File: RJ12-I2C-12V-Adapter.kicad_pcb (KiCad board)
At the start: 2 copper layers, 25.4 x 45.7 mm, 8 parts, among them J1 6P6C, J10 I²C, J11 Relais-Power, J2 6P6C

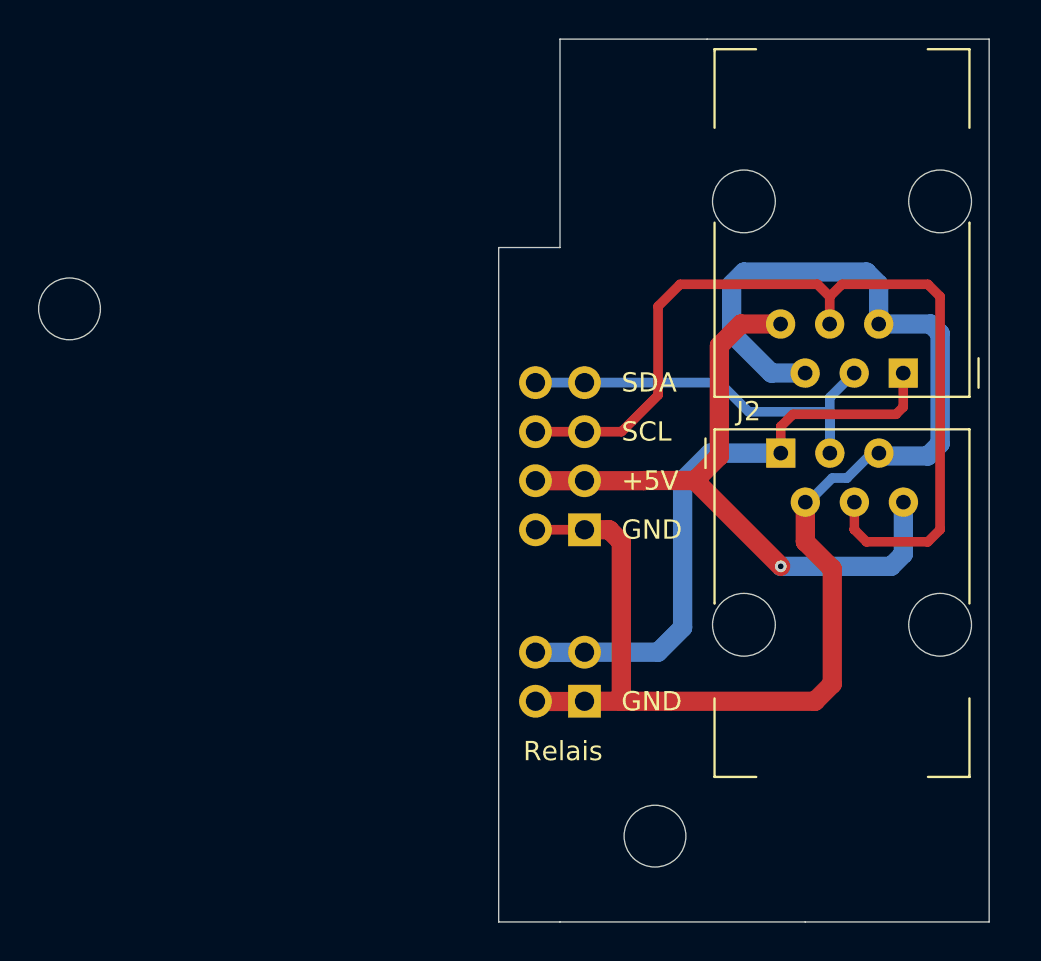
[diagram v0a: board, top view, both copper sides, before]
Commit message: Extra Anschlüsse für 12V/GND, RJ12 ganz an den Rand geschoben
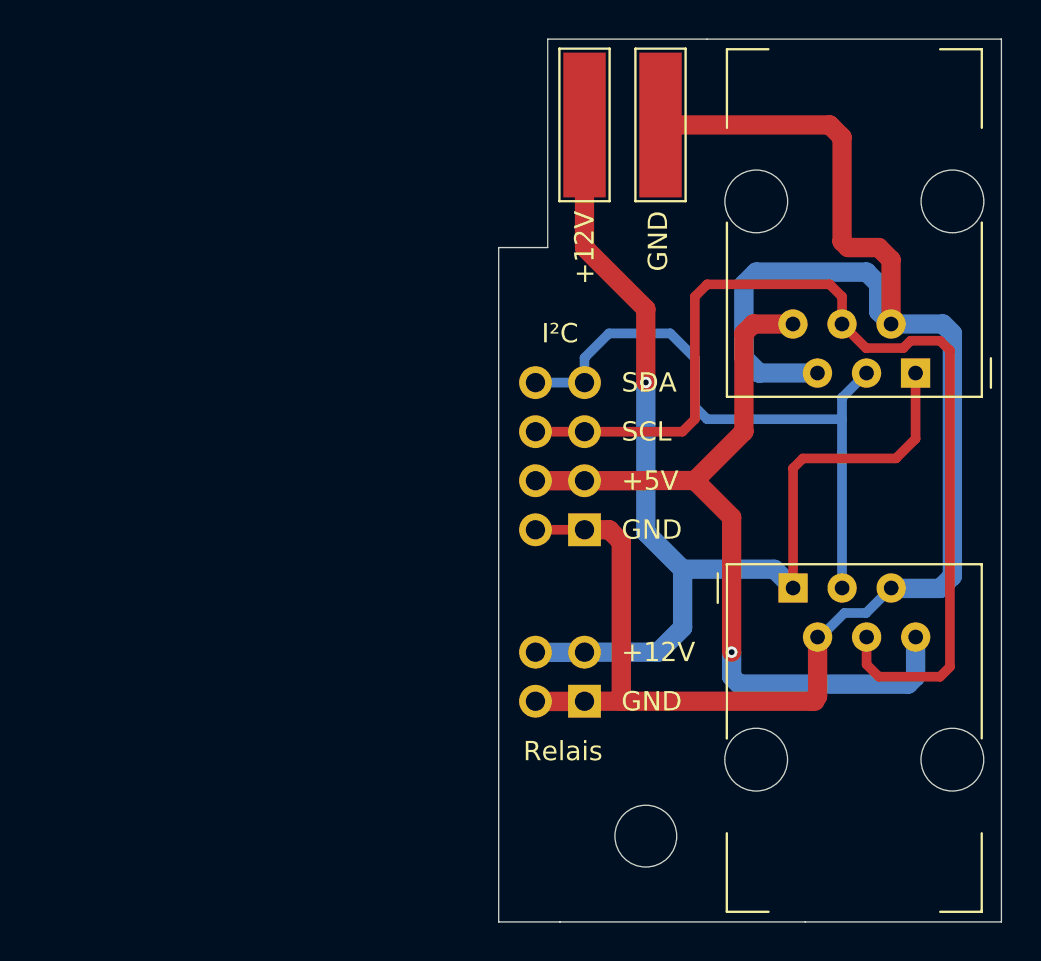
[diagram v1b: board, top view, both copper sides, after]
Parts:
- removed H1: MountingHole, MountingHole:MountingHole_3.2mm_M3
- added J12: +12V, Wago:Pad_7.5x2.2mm, F.Cu at (96.5, 71.8)
- added J13: GND, Wago:Pad_7.5x2.2mm, F.Cu at (100.5, 71.8)
- moved Tx1 21.1 mm to (81.3, 95.2)
- moved J2 7.01 mm to (107.3, 95.7)
- moved Tx2 3.67 mm to (106.7, 116.8)
- moved J1 0.64 mm to (113.7, 84.6)
- moved H2 0.48 mm to (99.7, 108.6)
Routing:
- net +12V: track 31.3 -> 59.0 mm, vias 0 -> 1
- net GND: track 73.4 -> 94.1 mm
- net /SDA: track 22.7 -> 32.7 mm
- net +5V: track 35.0 -> 42.4 mm
- net /SCL: track 47.5 -> 53.5 mm
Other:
- board size 25.4 x 45.7 mm -> 26 x 45.7 mm
- board text added: "+12V"

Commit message: Beschreibung J10/J10 geändert
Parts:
- J11: value Relais-Power -> Relais
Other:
- board text added: "I²C"
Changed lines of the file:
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@@
 		(tags "test point SMD pad rectangle square")
 		(property "Reference" "J12"
-			(at 0 -1.998 270)
+			(at 0 -1.998 -90)
 			(layer "F.SilkS")
 			(hide yes)
@@
 		)
 		(property "Value" "+12V"
-			(at -4.445 0 270)
+			(at -4.445 0 -90)
 			(layer "F.SilkS")
 			(effects
@@
 		)
 		(fp_text user "${REFERENCE}"
-			(at 0 -2.286 270)
+			(at 0 -2.286 -90)
 			(layer "F.Fab")
 			(hide yes)
@@
 		(tags "test point SMD pad rectangle square")
 		(property "Reference" "J13"
-			(at 0 -1.998 270)
+			(at 0 -1.998 -90)
 			(layer "F.SilkS")
 			(hide yes)
@@
 		)
 		(property "Value" "GND"
-			(at -4.445 -0.127 270)
+			(at -4.445 -0.127 -90)
 			(layer "F.SilkS")
 			(effects
@@
 		)
 		(fp_text user "${REFERENCE}"
-			(at 0 -2.286 270)
+			(at 0 -2.286 -90)
 			(layer "F.Fab")
 			(hide yes)
@@
 			(at -1.27 2.77 0)
 			(layer "B.SilkS")
+			(hide yes)
 			(effects
 				(font
@@
 			)
 		)
-		(property "Value" "Relais-Power"
-			(at -1.27 -5.31 0)
-			(layer "B.Fab")
-			(hide yes)
+		(property "Value" "Relais"
+			(at -1.27 2.54 0)
+			(layer "B.SilkS")
 			(effects
 				(font
@@
 			(at -1.27 2.77 0)
 			(layer "B.SilkS")
+			(hide yes)
 			(effects
 				(font
@@
 		(layer "Edge.Cuts")
 	)
+	(gr_text "I²C"
+		(at 95.885 83.185 0)
+		(layer "B.SilkS")
+		(effects
+			(font
+				(size 1 1)
+				(thickness 0.1)
+			)
+			(justify left bottom mirror)
+		)
+	)
 	(gr_text "GND"
